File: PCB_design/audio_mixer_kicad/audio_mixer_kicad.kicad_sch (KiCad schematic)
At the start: 122 parts, among them J1 B3B-XH-AMLFSN, J10 B3B-XH-AMLFSN, J11 B3B-XH-AMLFSN, J12 B3B-XH-AMLFSN, J13 B3B-XH-AMLFSN, J14 B3B-XH-AMLFSN, J15 B3B-XH-AMLFSN, J16 B3B-XH-AMLFSN, J17 B3B-XH-AMLFSN, J18 B3B-XH-AMLFSN, J19 B3B-XH-AMLFSN, J2 B3B-XH-AMLFSN, J20 B3B-XH-AMLFSN, J21 B3B-XH-AMLFSN, J22 B3B-XH-AMLFSN, J23 B3B-XH-AMLFSN, J24 B3B-XH-AMLFSN, J25 B3B-XH-AMLFSN, J26 B3B-XH-AMLFSN, J27 B3B-XH-AMLFSN, J28 B3B-XH-AMLFSN, J29 B3B-XH-AMLFSN, J3 B3B-XH-AMLFSN, J30 B3B-XH-AMLFSN, J31 B3B-XH-AMLFSN, J32 B3B-XH-AMLFSN, J33 Screw_Terminal_01x02, J34 B3B-XH-AMLFSN, J35 B3B-XH-AMLFSN, J36 B3B-XH-AMLFSN, J37 B3B-XH-AMLFSN, J4 B3B-XH-AMLFSN, J5 B3B-XH-AMLFSN, J6 B3B-XH-AMLFSN, J7 B3B-XH-AMLFSN, J8 B3B-XH-AMLFSN, J9 B3B-XH-AMLFSN, U1 XIAO-ESP32-S3-DIP, U2 Cmod A7-35T, Y1 24.576M

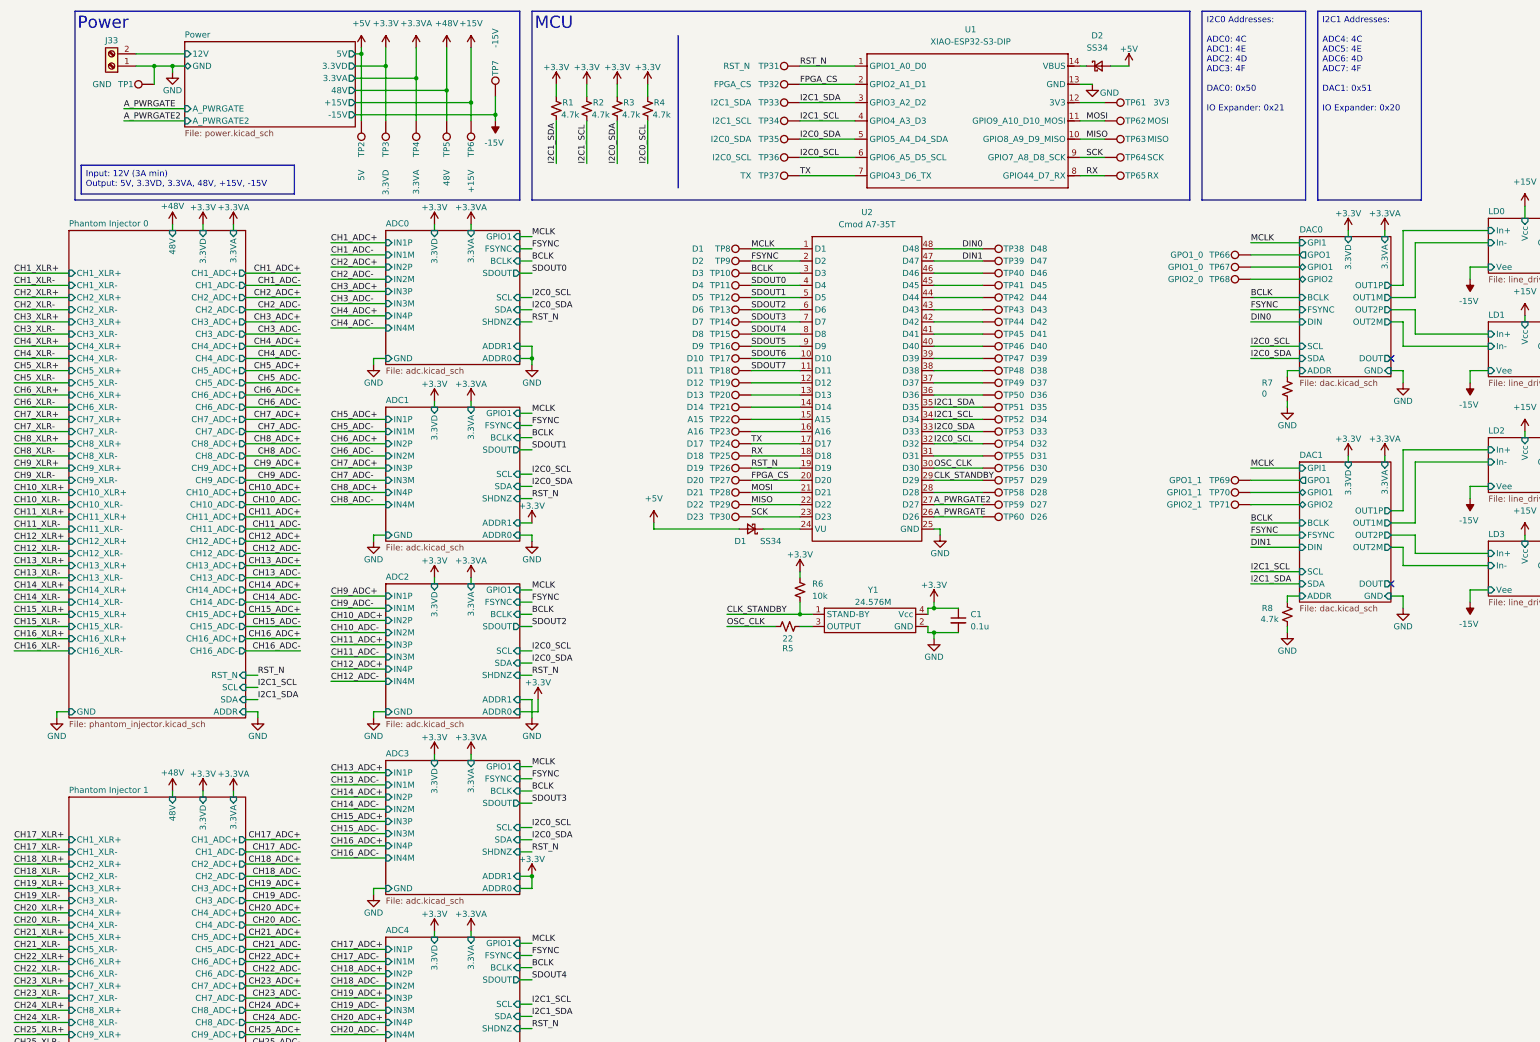
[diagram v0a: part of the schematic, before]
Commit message: Assign footprints
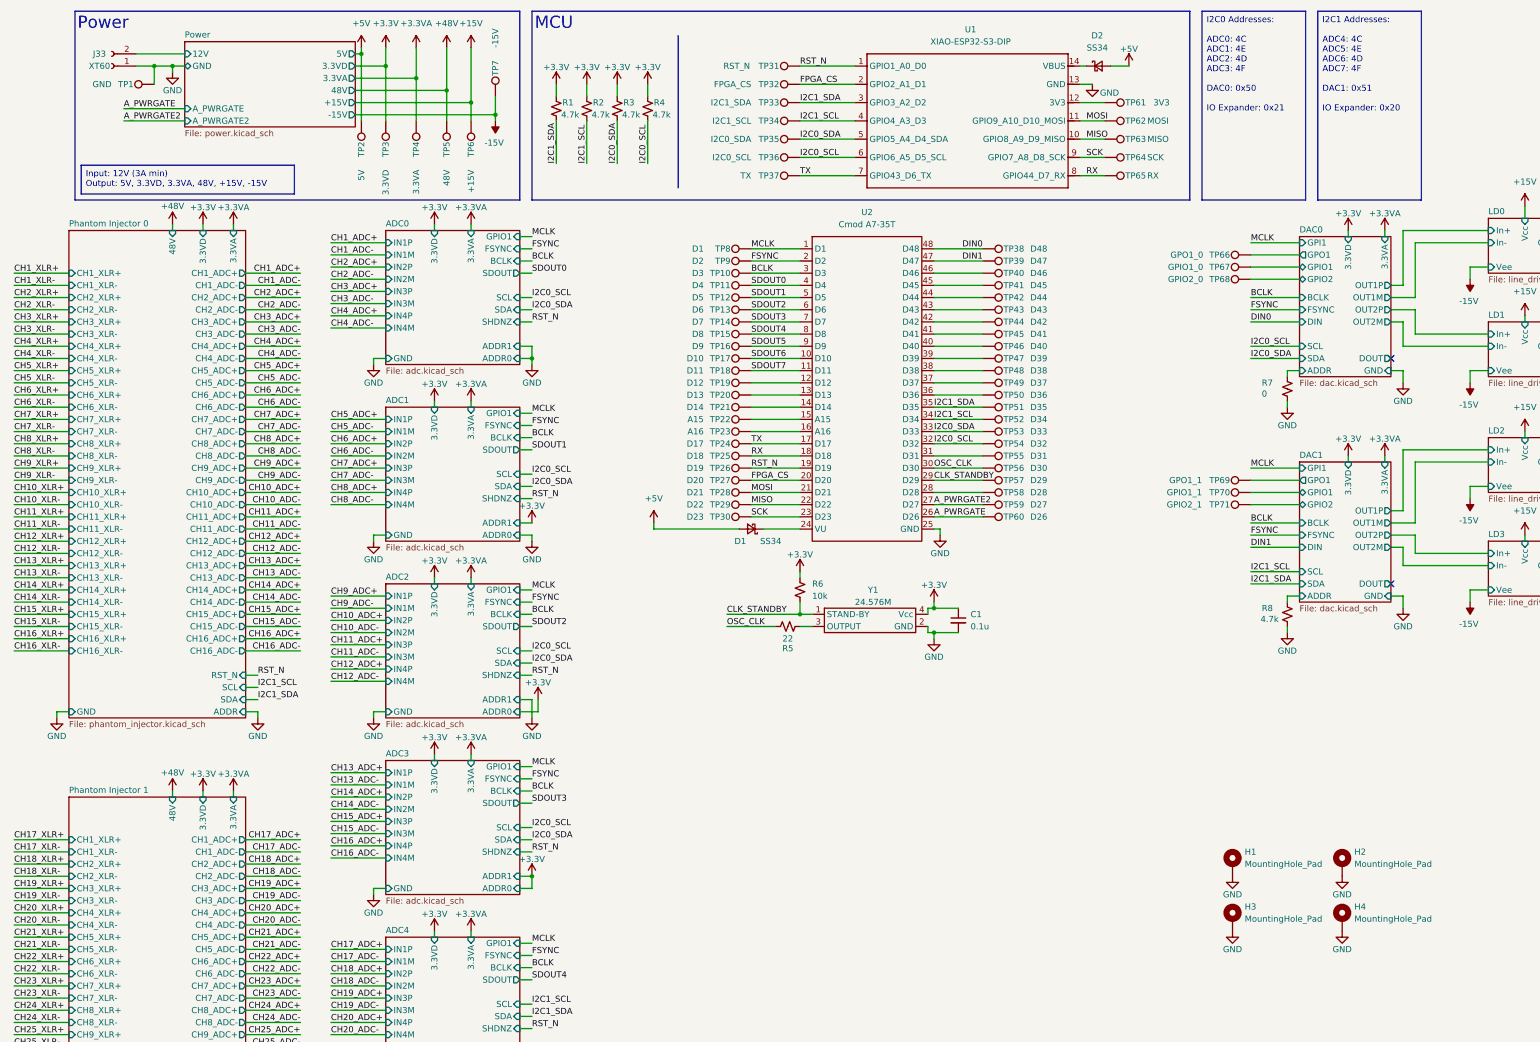
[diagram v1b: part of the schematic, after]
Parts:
- removed J33: Screw_Terminal_01x02, symbol Connector:Screw_Terminal_01x02
- added H1, H2, H3, H4: MountingHole_Pad, MountingHole:MountingHole_3.2mm_M3_Pad_TopBottom, symbol Mechanical:MountingHole_Pad
- added J33: XT60, Connector_AMASS:AMASS_XT60-M_1x02_P7.20mm_Vertical, symbol Connector:Conn_01x02_Socket
- C1: footprint (none) -> Capacitor_SMD:C_1206_3216Metric_Pad1.33x1.80mm_HandSolder
- D1, D2: footprint (none) -> SS34:DIOM7959X265N
- J1, J10, J11, J12, J13, J14, J15, J16, J17, J18, J19, J2, J20, J21, J22, J23, J24, J25, J26, J27, J28, J29, J3, J30, J31, J32, J34, J35, J36, J37, J4, J5, J6, J7, J8, J9: footprint CONN_B3B-XH-AMLFSN_JST -> JST_XH:CONN_B3B-XH-AMLFSN_JST
- R1, R2, R3, R4, R5, R6, R7, R8: footprint (none) -> Resistor_SMD:R_1206_3216Metric_Pad1.30x1.75mm_HandSolder
- TP1, TP10, TP11, TP12, TP13, TP14, TP15, TP16, TP17, TP18, TP19, TP2, TP20, TP21, TP22, TP23, TP24, TP25, TP26, TP27, TP28, TP29, TP3, TP30, TP31, TP32, TP33, TP34, TP35, TP36, TP37, TP38, TP39, TP4, TP40, TP41, TP42, TP43, TP44, TP45, TP46, TP47, TP48, TP49, TP5, TP50, TP51, TP52, TP53, TP54, TP55, TP56, TP57, TP58, TP59, TP6, TP60, TP61, TP62, TP63, TP64, TP65, TP66, TP67, TP68, TP69, TP7, TP70, TP71, TP8, TP9: footprint (none) -> TestPoint:TestPoint_THTPad_D2.0mm_Drill1.0mm
- U1: footprint Seeed_Studio_XIAO_Series:XIAO-ESP32-S3-DIP -> XIAO_footprint:XIAO-ESP32-S3-DIP
- U2: footprint (none) -> audio_mixer_footprints:Cmod-A7
- Y1: footprint (none) -> audio_mixer_footprints:NZ2520SDA
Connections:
- net GND: now also H1.1, H2.1, H3.1, H4.1, J33.1 (Pin_1)
- net Power/12V: now also J33.2 (Pin_2)
